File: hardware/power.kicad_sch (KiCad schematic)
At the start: 2 parts, among them P8 Conn_01x06, P9 Conn_01x06

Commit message: getting closer
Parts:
- added J12: Conn_01x02, symbol Connector_Generic:Conn_01x02
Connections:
- net GND: now also J12.2 (Pin_2)
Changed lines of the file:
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@@
 (kicad_sch (version 20230121) (generator eeschema)
   (paper "A4")
+  (junction (at 127 88.9) (diameter 0) (color 0 0 0 0)
+  )
   (junction (at 132.08 88.9) (diameter 0) (color 0 0 0 0)
   )
+  (junction (at 111.76 88.9) (diameter 0) (color 0 0 0 0)
+  )
   (junction (at 116.84 88.9) (diameter 0) (color 0 0 0 0)
   )
@@
   (junction (at 124.46 88.9) (diameter 0) (color 0 0 0 0)
   )
+  (junction (at 114.3 88.9) (diameter 0) (color 0 0 0 0)
+  )
   (wire (pts (xy 119.38 99.06) (xy 116.84 99.06))
     (stroke (width 0) (type default))
@@
     (stroke (width 0) (type default))
   )
+  (wire (pts (xy 190.5 96.52) (xy 187.96 96.52))
+    (stroke (width 0) (type default))
+  )
   (wire (pts (xy 116.84 88.9) (xy 116.84 99.06))
     (stroke (width 0) (type default))
@@
     (stroke (width 0) (type default))
   )
+  (wire (pts (xy 114.3 88.9) (xy 114.3 106.68))
+    (stroke (width 0) (type default))
+  )
   (wire (pts (xy 127 86.36) (xy 127 88.9))
     (stroke (width 0) (type default))
@@
     (stroke (width 0) (type default))
   )
+  (wire (pts (xy 134.62 88.9) (xy 134.62 101.6))
+    (stroke (width 0) (type default))
+  )
   (wire (pts (xy 132.08 88.9) (xy 129.54 88.9))
     (stroke (width 0) (type default))
@@
     (stroke (width 0) (type default))
   )
+  (wire (pts (xy 127 88.9) (xy 127 106.68))
+    (stroke (width 0) (type default))
+  )
+  (wire (pts (xy 187.96 96.52) (xy 187.96 101.6))
+    (stroke (width 0) (type default))
+  )
   (wire (pts (xy 124.46 99.06) (xy 119.38 99.06))
+    (stroke (width 0) (type default))
+  )
+  (wire (pts (xy 111.76 88.9) (xy 111.76 114.3))
     (stroke (width 0) (type default))
   )
@@
         (path "/3006deba-2100-40f8-9f39-987a5c2c14c7/f8ecdba8-12ed-4532-a81b-3b086d58d046"
           (reference "#PWR013") (unit 1)
+        )
+      )
+    )
+  )
+  (symbol (lib_id "Connector_Generic:Conn_01x02") (at 195.58 93.98 0) (unit 1)
+    (in_bom yes) (on_board yes) (dnp no) (fields_autoplaced)
+    (property "Reference" "J12" (at 198.12 93.98 0)
+      (effects (font (size 1.27 1.27)) (justify left))
+    )
+    (property "Value" "Conn_01x02" (at 198.12 96.52 0)
+      (effects (font (size 1.27 1.27)) (justify left))
+    )
+    (property "Footprint" "" (at 195.58 93.98 0)
+      (effects (font (size 1.27 1.27)) hide)
+    )
+    (property "Datasheet" "~" (at 195.58 93.98 0)
+      (effects (font (size 1.27 1.27)) hide)
+    )
+    (pin "2")
+    (pin "1")
+    (instances
+      (project "68040pc"
+        (path "/3006deba-2100-40f8-9f39-987a5c2c14c7/f8ecdba8-12ed-4532-a81b-3b086d58d046"
+          (reference "J12") (unit 1)
         )
       )
@@
     )
   )
+  (symbol (lib_id "power:PWR_FLAG") (at 114.3 106.68 0) (mirror x) (unit 1)
+    (in_bom yes) (on_board yes) (dnp no) (fields_autoplaced)
+    (property "Reference" "#FLG04" (at 114.3 108.585 0)
+      (effects (font (size 1.27 1.27)) hide)
+    )
+    (property "Value" "PWR_FLAG" (at 114.3 111.76 0)
+      (effects (font (size 1.27 1.27)))
+    )
+    (property "Footprint" "" (at 114.3 106.68 0)
+      (effects (font (size 1.27 1.27)) hide)
+    )
+    (property "Datasheet" "~" (at 114.3 106.68 0)
+      (effects (font (size 1.27 1.27)) hide)
+    )
+    (pin "1")
+    (instances
+      (project "68040pc"
+        (path "/3006deba-2100-40f8-9f39-987a5c2c14c7/f8ecdba8-12ed-4532-a81b-3b086d58d046"
+          (reference "#FLG04") (unit 1)
+        )
+      )
+    )
+  )
   (symbol (lib_id "power:GND") (at 119.38 101.6 0) (unit 1)
     (in_bom yes) (on_board yes) (dnp no) (fields_autoplaced)
@@
         (path "/3006deba-2100-40f8-9f39-987a5c2c14c7/f8ecdba8-12ed-4532-a81b-3b086d58d046"
           (reference "#PWR014") (unit 1)
+        )
+      )
+    )
+  )
+  (symbol (lib_id "power:PWR_FLAG") (at 134.62 101.6 0) (mirror x) (unit 1)
+    (in_bom yes) (on_board yes) (dnp no) (fields_autoplaced)
+    (property "Reference" "#FLG02" (at 134.62 103.505 0)
+      (effects (font (size 1.27 1.27)) hide)
+    )
+    (property "Value" "PWR_FLAG" (at 134.62 106.68 0)
+      (effects (font (size 1.27 1.27)))
+    )
+    (property "Footprint" "" (at 134.62 101.6 0)
+      (effects (font (size 1.27 1.27)) hide)
+    )
+    (property "Datasheet" "~" (at 134.62 101.6 0)
+      (effects (font (size 1.27 1.27)) hide)
+    )
+    (pin "1")
+    (instances
+      (project "68040pc"
+        (path "/3006deba-2100-40f8-9f39-987a5c2c14c7/f8ecdba8-12ed-4532-a81b-3b086d58d046"
+          (reference "#FLG02") (unit 1)
+        )
+      )
+    )
+  )
+  (symbol (lib_id "power:PWR_FLAG") (at 111.76 114.3 0) (mirror x) (unit 1)
+    (in_bom yes) (on_board yes) (dnp no) (fields_autoplaced)
+    (property "Reference" "#FLG01" (at 111.76 116.205 0)
+      (effects (font (size 1.27 1.27)) hide)
+    )
+    (property "Value" "PWR_FLAG" (at 111.76 119.38 0)
+      (effects (font (size 1.27 1.27)))
+    )
+    (property "Footprint" "" (at 111.76 114.3 0)
+      (effects (font (size 1.27 1.27)) hide)
+    )
+    (property "Datasheet" "~" (at 111.76 114.3 0)
+      (effects (font (size 1.27 1.27)) hide)
+    )
+    (pin "1")
+    (instances
+      (project "68040pc"
+        (path "/3006deba-2100-40f8-9f39-987a5c2c14c7/f8ecdba8-12ed-4532-a81b-3b086d58d046"
+          (reference "#FLG01") (unit 1)
         )
       )
@@
     )
   )
+  (symbol (lib_id "power:PWR_FLAG") (at 127 106.68 0) (mirror x) (unit 1)
+    (in_bom yes) (on_board yes) (dnp no) (fields_autoplaced)
+    (property "Reference" "#FLG03" (at 127 108.585 0)
+      (effects (font (size 1.27 1.27)) hide)
+    )
+    (property "Value" "PWR_FLAG" (at 127 111.76 0)
+      (effects (font (size 1.27 1.27)))
+    )
+    (property "Footprint" "" (at 127 106.68 0)
+      (effects (font (size 1.27 1.27)) hide)
+    )
+    (property "Datasheet" "~" (at 127 106.68 0)
+      (effects (font (size 1.27 1.27)) hide)
+    )
+    (pin "1")
+    (instances
+      (project "68040pc"
+        (path "/3006deba-2100-40f8-9f39-987a5c2c14c7/f8ecdba8-12ed-4532-a81b-3b086d58d046"
+          (reference "#FLG03") (unit 1)
+        )
+      )
+    )
+  )
   (symbol (lib_id "power:+5V") (at 109.22 88.9 0) (unit 1)
     (in_bom yes) (on_board yes) (dnp no) (fields_autoplaced)
@@
         )
       )
+    )
+  )
+  (symbol (lib_id "power:GND") (at 187.96 101.6 0) (unit 1)
+    (in_bom yes) (on_board yes) (dnp no) (fields_autoplaced)
+    (property "Reference" "#PWR014" (at 187.96 107.95 0)
+      (effects (font (size 1.27 1.27)) hide)
+    )
+    (property "Value" "GND" (at 187.96 106.68 0)
+      (effects (font (size 1.27 1.27)))
+    )
+    (property "Footprint" "" (at 187.96 101.6 0)
+      (effects (font (size 1.27 1.27)) hide)
+    )
+    (property "Datasheet" "" (at 187.96 101.6 0)
+      (effects (font (size 1.27 1.27)) hide)
+    )
+    (pin "1")
+    (instances
+      (project "68040pc"
+        (path "/3006deba-2100-40f8-9f39-987a5c2c14c7"
+          (reference "#PWR014") (unit 1)
+        )
+        (path "/3006deba-2100-40f8-9f39-987a5c2c14c7/f8ecdba8-12ed-4532-a81b-3b086d58d046"
+          (reference "#PWR032") (unit 1)
+        )
+      )

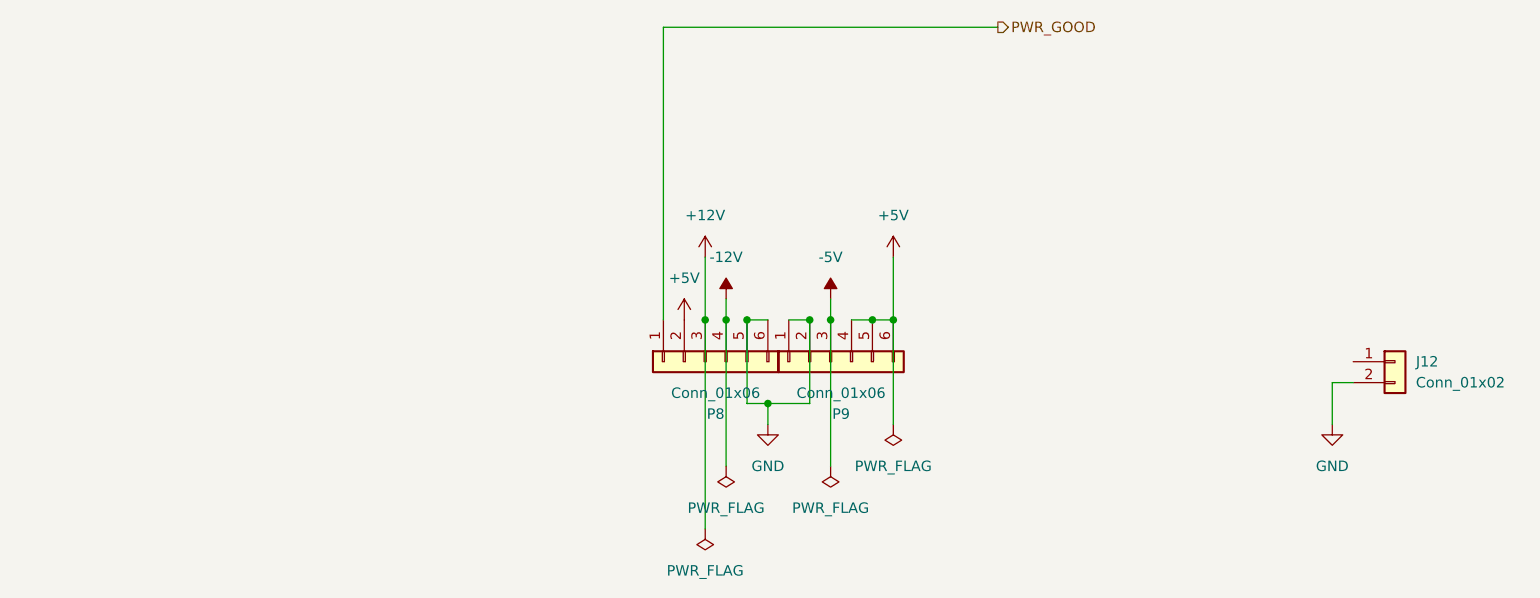
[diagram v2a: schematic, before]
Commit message: re-design level shifters
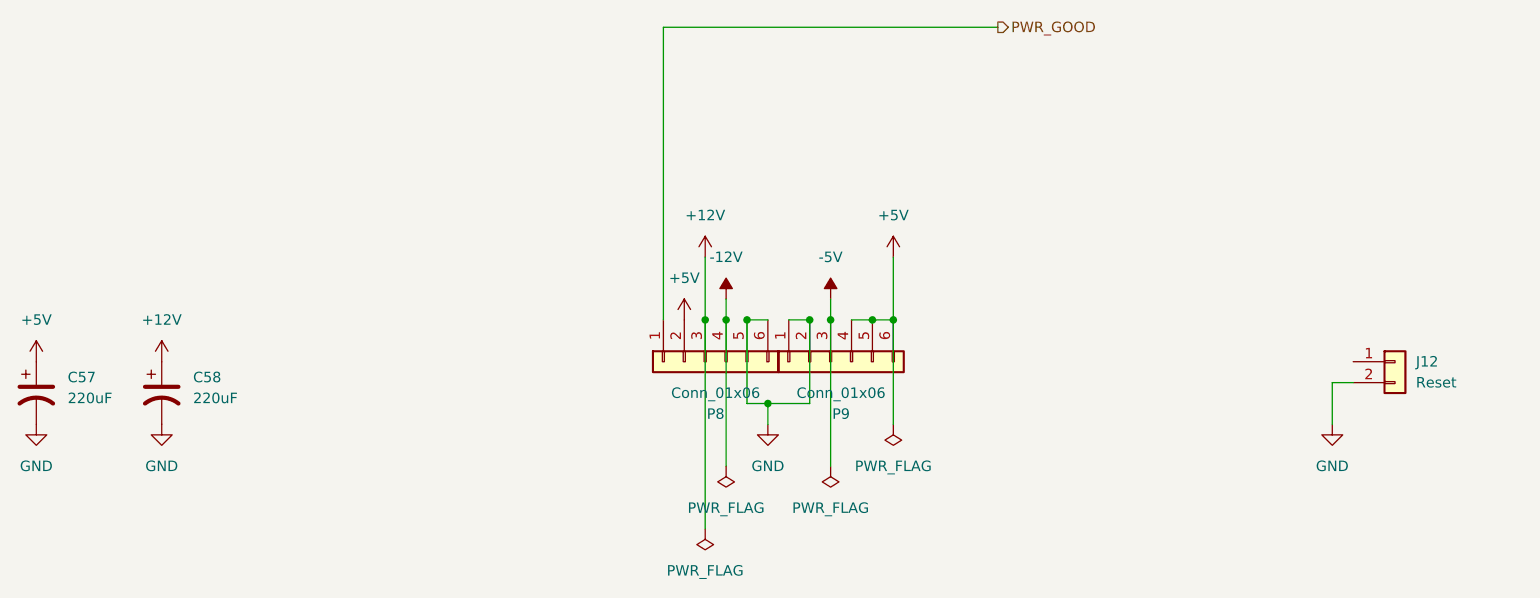
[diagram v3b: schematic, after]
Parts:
- added C57, C58: 220uF, symbol Device:C_Polarized_US
- J12: value Conn_01x02 -> Reset; footprint (none) -> Connector_PinHeader_2.54mm:PinHeader_1x02_P2.54mm_Vertical
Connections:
- net +12V: now also C58.1
- net +5V: now also C57.1
- net GND: now also C57.2, C58.2
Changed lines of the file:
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@@
+    )
+  )
+  (symbol (lib_id "power:GND") (at 30.48 101.6 0) (unit 1)
+    (in_bom yes) (on_board yes) (dnp no) (fields_autoplaced)
+    (property "Reference" "#PWR014" (at 30.48 107.95 0)
+      (effects (font (size 1.27 1.27)) hide)
+    )
+    (property "Value" "GND" (at 30.48 106.68 0)
+      (effects (font (size 1.27 1.27)))
+    )
+    (property "Footprint" "" (at 30.48 101.6 0)
+      (effects (font (size 1.27 1.27)) hide)
+    )
+    (property "Datasheet" "" (at 30.48 101.6 0)
+      (effects (font (size 1.27 1.27)) hide)
+    )
+    (pin "1")
+    (instances
+      (project "68040pc"
+        (path "/3006deba-2100-40f8-9f39-987a5c2c14c7"
+          (reference "#PWR014") (unit 1)
+        )
+        (path "/3006deba-2100-40f8-9f39-987a5c2c14c7/f8ecdba8-12ed-4532-a81b-3b086d58d046"
+          (reference "#PWR0201") (unit 1)
+        )
+      )
     )
   )
@@
       (effects (font (size 1.27 1.27)) (justify left))
     )
-    (property "Value" "Conn_01x02" (at 198.12 96.52 0)
-      (effects (font (size 1.27 1.27)) (justify left))
-    )
-    (property "Footprint" "" (at 195.58 93.98 0)
+    (property "Value" "Reset" (at 198.12 96.52 0)
+      (effects (font (size 1.27 1.27)) (justify left))
+    )
+    (property "Footprint" "Connector_PinHeader_2.54mm:PinHeader_1x02_P2.54mm_Vertical" (at 195.58 93.98 0)
       (effects (font (size 1.27 1.27)) hide)
     )
@@
     )
   )
+  (symbol (lib_id "Device:C_Polarized_US") (at 30.48 97.79 0) (unit 1)
+    (in_bom yes) (on_board yes) (dnp no) (fields_autoplaced)
+    (property "Reference" "C57" (at 34.29 95.885 0)
+      (effects (font (size 1.27 1.27)) (justify left))
+    )
+    (property "Value" "220uF" (at 34.29 98.425 0)
+      (effects (font (size 1.27 1.27)) (justify left))
+    )
+    (property "Footprint" "" (at 30.48 97.79 0)
+      (effects (font (size 1.27 1.27)) hide)
+    )
+    (property "Datasheet" "~" (at 30.48 97.79 0)
+      (effects (font (size 1.27 1.27)) hide)
+    )
+    (pin "2")
+    (pin "1")
+    (instances
+      (project "68040pc"
+        (path "/3006deba-2100-40f8-9f39-987a5c2c14c7/f8ecdba8-12ed-4532-a81b-3b086d58d046"
+          (reference "C57") (unit 1)
+        )
+      )
+    )
+  )
   (symbol (lib_id "power:-5V") (at 127 86.36 0) (unit 1)
     (in_bom yes) (on_board yes) (dnp no) (fields_autoplaced)
@@
         (path "/3006deba-2100-40f8-9f39-987a5c2c14c7/f8ecdba8-12ed-4532-a81b-3b086d58d046"
           (reference "#FLG02") (unit 1)
+        )
+      )
+    )
+  )
+  (symbol (lib_id "power:+12V") (at 45.72 93.98 0) (unit 1)
+    (in_bom yes) (on_board yes) (dnp no) (fields_autoplaced)
+    (property "Reference" "#PWR012" (at 45.72 97.79 0)
+      (effects (font (size 1.27 1.27)) hide)
+    )
+    (property "Value" "+12V" (at 45.72 88.9 0)
+      (effects (font (size 1.27 1.27)))
+    )
+    (property "Footprint" "" (at 45.72 93.98 0)
+      (effects (font (size 1.27 1.27)) hide)
+    )
+    (property "Datasheet" "" (at 45.72 93.98 0)
+      (effects (font (size 1.27 1.27)) hide)
+    )
+    (pin "1")
+    (instances
+      (project "68040pc"
+        (path "/3006deba-2100-40f8-9f39-987a5c2c14c7"
+          (reference "#PWR012") (unit 1)
+        )
+        (path "/3006deba-2100-40f8-9f39-987a5c2c14c7/f8ecdba8-12ed-4532-a81b-3b086d58d046"
+          (reference "#PWR0202") (unit 1)
         )
       )
@@
         )
       )
+    )
+  )
+  (symbol (lib_id "Device:C_Polarized_US") (at 45.72 97.79 0) (unit 1)
+    (in_bom yes) (on_board yes) (dnp no) (fields_autoplaced)
+    (property "Reference" "C58" (at 49.53 95.885 0)
+      (effects (font (size 1.27 1.27)) (justify left))
+    )
+    (property "Value" "220uF" (at 49.53 98.425 0)
+      (effects (font (size 1.27 1.27)) (justify left))
+    )
+    (property "Footprint" "" (at 45.72 97.79 0)
+      (effects (font (size 1.27 1.27)) hide)
+    )
+    (property "Datasheet" "~" (at 45.72 97.79 0)
+      (effects (font (size 1.27 1.27)) hide)
+    )
+    (pin "2")
+    (pin "1")
+    (instances
+      (project "68040pc"
+        (path "/3006deba-2100-40f8-9f39-987a5c2c14c7/f8ecdba8-12ed-4532-a81b-3b086d58d046"
+          (reference "C58") (unit 1)
+        )
+      )
+    )
+  )
+  (symbol (lib_id "power:+5V") (at 30.48 93.98 0) (unit 1)
+    (in_bom yes) (on_board yes) (dnp no) (fields_autoplaced)
+    (property "Reference" "#PWR016" (at 30.48 97.79 0)
+      (effects (font (size 1.27 1.27)) hide)
+    )
+    (property "Value" "+5V" (at 30.48 88.9 0)
+      (effects (font (size 1.27 1.27)))
+    )
+    (property "Footprint" "" (at 30.48 93.98 0)
+      (effects (font (size 1.27 1.27)) hide)
+    )
+    (property "Datasheet" "" (at 30.48 93.98 0)
+      (effects (font (size 1.27 1.27)) hide)
+    )
+    (pin "1")
+    (instances
+      (project "68040pc"
+        (path "/3006deba-2100-40f8-9f39-987a5c2c14c7"
+          (reference "#PWR016") (unit 1)
+        )
+        (path "/3006deba-2100-40f8-9f39-987a5c2c14c7/f8ecdba8-12ed-4532-a81b-3b086d58d046"
+          (reference "#PWR0200") (unit 1)
+        )
+      )
+    )
+  )
+  (symbol (lib_id "power:GND") (at 45.72 101.6 0) (unit 1)
+    (in_bom yes) (on_board yes) (dnp no) (fields_autoplaced)
+    (property "Reference" "#PWR014" (at 45.72 107.95 0)
+      (effects (font (size 1.27 1.27)) hide)
+    )
+    (property "Value" "GND" (at 45.72 106.68 0)
+      (effects (font (size 1.27 1.27)))
+    )
+    (property "Footprint" "" (at 45.72 101.6 0)
+      (effects (font (size 1.27 1.27)) hide)
+    )
+    (property "Datasheet" "" (at 45.72 101.6 0)
+      (effects (font (size 1.27 1.27)) hide)
+    )
+    (pin "1")
+    (instances
+      (project "68040pc"
+        (path "/3006deba-2100-40f8-9f39-987a5c2c14c7"
+          (reference "#PWR014") (unit 1)
+        )
+        (path "/3006deba-2100-40f8-9f39-987a5c2c14c7/f8ecdba8-12ed-4532-a81b-3b086d58d046"
+          (reference "#PWR0203") (unit 1)
+        )
+      )
